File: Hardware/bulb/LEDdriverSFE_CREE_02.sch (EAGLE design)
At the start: 26 parts, among them U1 ZXLD1360, U2 ZXLD1360, U3 ZXLD1360, U4 ZXLD1360

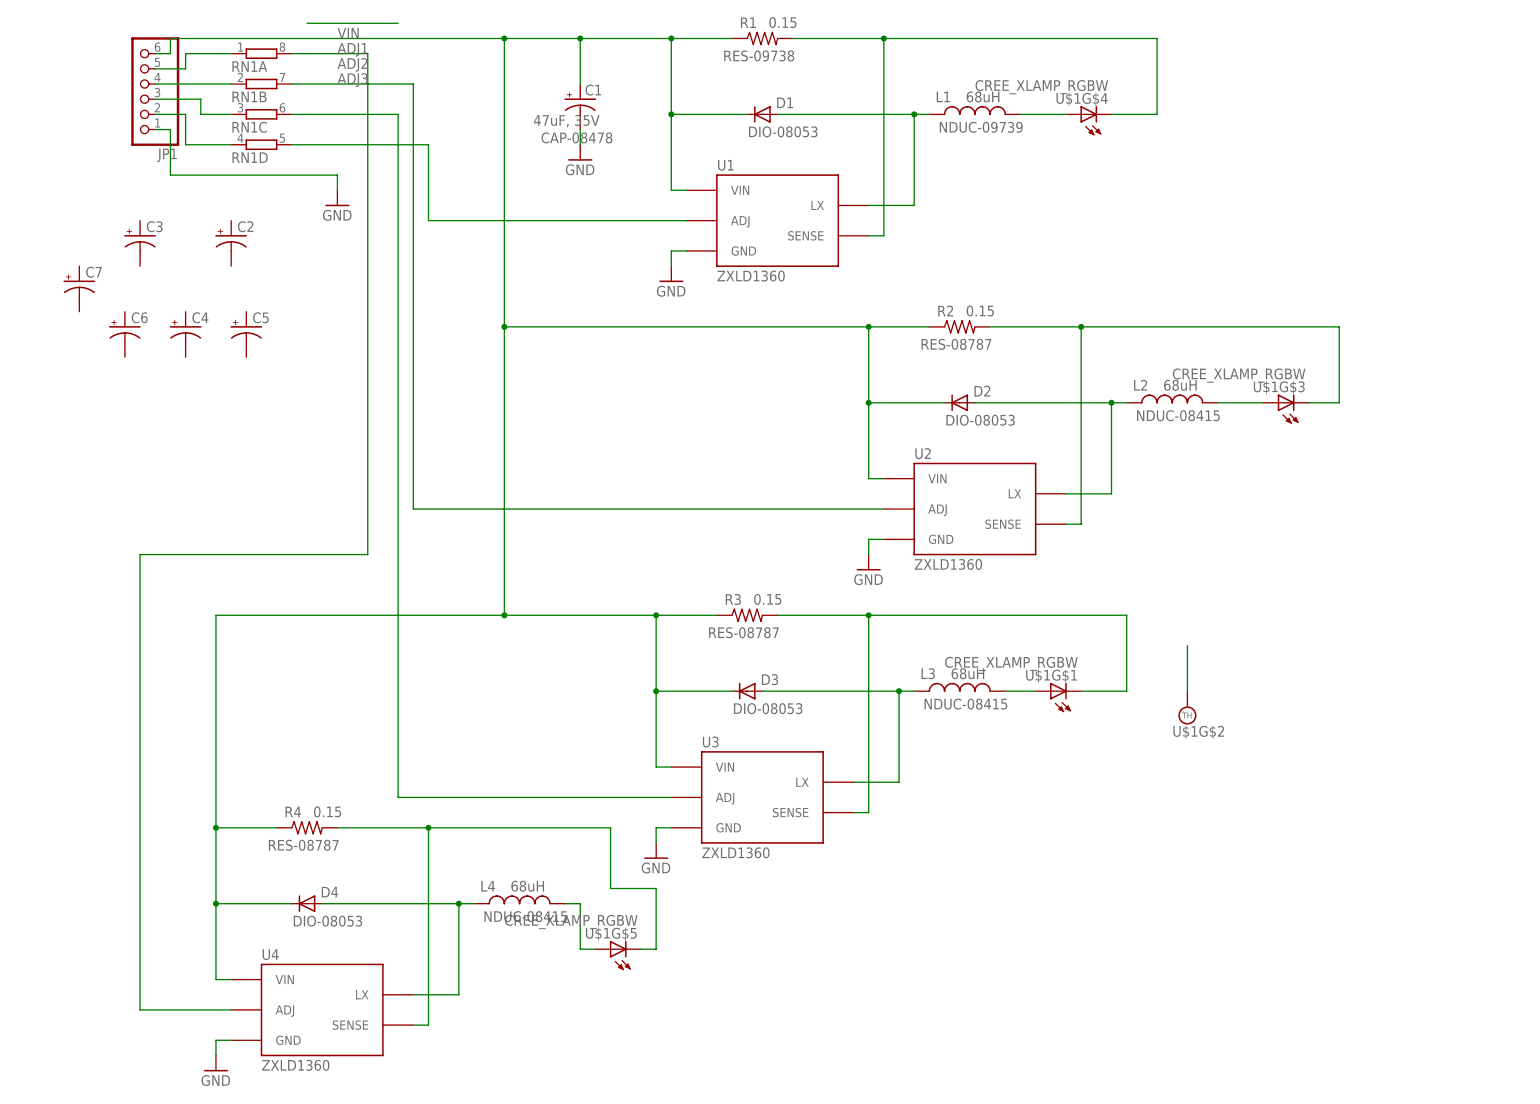
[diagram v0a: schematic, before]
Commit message: added firmware version 08 and included updates to server
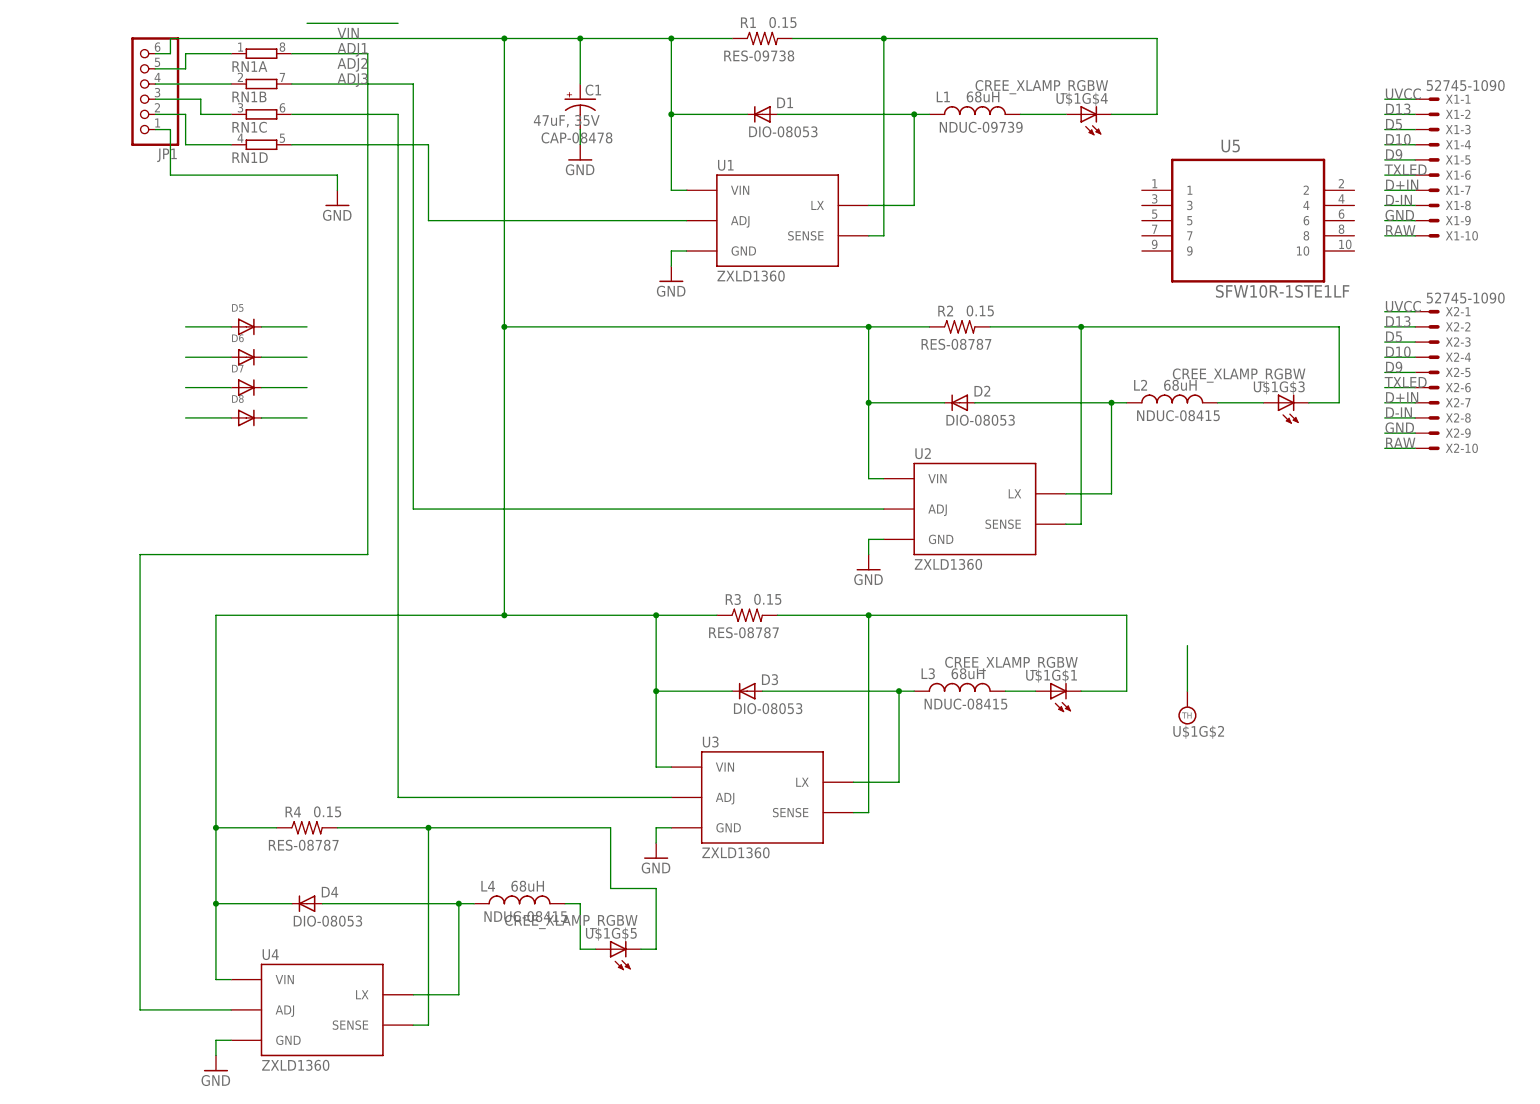
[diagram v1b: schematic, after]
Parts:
- removed C2: (no value), rcl:CPOL-USB
- removed C3: (no value), rcl:CPOL-US153CLV-0605
- removed C4: (no value), rcl:CPOL-US153CLV-0505
- removed C5: (no value), rcl:CPOL-USC
- removed C6: (no value), rcl:CPOL-US153CLV-0807
- removed C7: (no value), rcl:CPOL-US175TMP-0808
- added D5, D6, D7, D8: (no value), adafruit:DIODESOD-323F
- added U5: SFW10R-1STE1LF, FCI_By_element14_Batch_1:SFW10R-1STE1LF
- added X1, X2: 52745-1090, con-molex:52745-1090
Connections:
- removed net N$15: JP1.5, RN1A.1
- removed net N$18: JP1.3, RN1C.1
- new net BLUEIN: D7.C, JP1.4, RN1B.1
- new net D+IN: X1-7.S, X2-7.S
- new net D-IN: X1-8.S, X2-8.S
- new net D10: X1-4.S, X2-4.S
- new net D13: X1-2.S, X2-2.S
- new net D5: X1-3.S, X2-3.S
- new net D9: X1-5.S, X2-5.S
- new net GREENIN: D6.C, JP1.2, RN1D.1
- new net N$20: D7.A
- new net N$21: D8.A
- new net RAW: X1-10.S, X2-10.S
- new net REDIN: D5.C, JP1.5, RN1A.1
- new net TXLED: X1-6.S, X2-6.S
- new net UVCC: X1-1.S, X2-1.S
- new net WHITEIN: D8.C, JP1.3, RN1C.1
- net GND: now also X1-9.S, X2-9.S
- net N$14: now also D5.A; no longer JP1.2, RN1D.1
- net N$17: now also D6.A; no longer JP1.4, RN1B.1
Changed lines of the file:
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@@
 <?xml version="1.0" encoding="utf-8"?>
 <!DOCTYPE eagle SYSTEM "eagle.dtd">
-<eagle version="6.2">
+<eagle version="6.4">
 <drawing>
 <settings>
@@
 <class number="0" name="default" width="0" drill="0">
 </class>
+<class number="1" name="vcc" width="0" drill="0">
+</class>
 </classes>
 <parts>
@@
 <part name="JP1" library="adafruit" deviceset="PINHD-1X6" device=""/>
 <part name="RN1" library="resistor-dil" deviceset="4R-N" device="EXBV8V"/>
-<part name="C2" library="rcl" deviceset="CPOL-US" device="B"/>
-<part name="C3" library="rcl" deviceset="CPOL-US" device="153CLV-0605"/>
-<part name="C4" library="rcl" deviceset="CPOL-US" device="153CLV-0505"/>
-<part name="C5" library="rcl" deviceset="CPOL-US" device="C"/>
-<part name="C6" library="rcl" deviceset="CPOL-US" device="153CLV-0807"/>
-<part name="C7" library="rcl" deviceset="CPOL-US" device="175TMP-0808"/>
+<part name="D5" library="adafruit" deviceset="DIODE" device="SOD-323F"/>
+<part name="D6" library="adafruit" deviceset="DIODE" device="SOD-323F"/>
+<part name="D7" library="adafruit" deviceset="DIODE" device="SOD-323F"/>
+<part name="D8" library="adafruit" deviceset="DIODE" device="SOD-323F"/>
+<part name="X1" library="con-molex" deviceset="52745-1090" device=""/>
+<part name="X2" library="con-molex" deviceset="52745-1090" device=""/>
+<part name="U5" library="FCI_By_element14_Batch_1" deviceset="SFW10R-1STE1LF" device=""/>
 </parts>
 <sheets>
@@
 <instance part="RN1" gate="C" x="35.56" y="165.1"/>
 <instance part="RN1" gate="D" x="35.56" y="160.02"/>
-<instance part="C2" gate="G$1" x="30.48" y="144.78"/>
-<instance part="C3" gate="G$1" x="15.24" y="144.78"/>
-<instance part="C4" gate="G$1" x="22.86" y="129.54"/>
-<instance part="C5" gate="G$1" x="33.02" y="129.54"/>
-<instance part="C6" gate="G$1" x="12.7" y="129.54"/>
-<instance part="C7" gate="G$1" x="5.08" y="137.16"/>
+<instance part="D5" gate="G$1" x="33.02" y="129.54"/>
+<instance part="D6" gate="G$1" x="33.02" y="124.46"/>
+<instance part="D7" gate="G$1" x="33.02" y="119.38"/>
+<instance part="D8" gate="G$1" x="33.02" y="114.3"/>
+<instance part="X1" gate="-1" x="231.14" y="167.64"/>
+<instance part="X1" gate="-2" x="231.14" y="165.1"/>
+<instance part="X1" gate="-3" x="231.14" y="162.56"/>
+<instance part="X1" gate="-4" x="231.14" y="160.02"/>
+<instance part="X1" gate="-5" x="231.14" y="157.48"/>
+<instance part="X1" gate="-6" x="231.14" y="154.94"/>
+<instance part="X1" gate="-7" x="231.14" y="152.4"/>
+<instance part="X1" gate="-8" x="231.14" y="149.86"/>
+<instance part="X1" gate="-9" x="231.14" y="147.32"/>
+<instance part="X1" gate="-10" x="231.14" y="144.78"/>
+<instance part="X2" gate="-1" x="231.14" y="132.08"/>
+<instance part="X2" gate="-2" x="231.14" y="129.54"/>
+<instance part="X2" gate="-3" x="231.14" y="127"/>
+<instance part="X2" gate="-4" x="231.14" y="124.46"/>
+<instance part="X2" gate="-5" x="231.14" y="121.92"/>
+<instance part="X2" gate="-6" x="231.14" y="119.38"/>
+<instance part="X2" gate="-7" x="231.14" y="116.84"/>
+<instance part="X2" gate="-8" x="231.14" y="114.3"/>
+<instance part="X2" gate="-9" x="231.14" y="111.76"/>
+<instance part="X2" gate="-10" x="231.14" y="109.22"/>
+<instance part="U5" gate="A" x="200.66" y="149.86"/>
 </instances>
 <busses>
@@
 <pinref part="U4" gate="G$1" pin="GND"/>
 <pinref part="GND6" gate="1" pin="GND"/>
+</segment>
+<segment>
+<pinref part="X1" gate="-9" pin="S"/>
+<wire x1="228.6" y1="147.32" x2="223.52" y2="147.32" width="0.1524" layer="91"/>
+<label x="223.52" y="147.32" size="1.778" layer="95"/>
+</segment>
+<segment>
+<pinref part="X2" gate="-9" pin="S"/>
+<wire x1="228.6" y1="111.76" x2="223.52" y2="111.76" width="0.1524" layer="91"/>
+<label x="223.52" y="111.76" size="1.778" layer="95"/>
 </segment>
 </net>
@@
 </segment>
 </net>
-<net name="N$14" class="0">
+<net name="GREENIN" class="0">
 <segment>
 <pinref part="RN1" gate="D" pin="1"/>
@@
 <wire x1="22.86" y1="165.1" x2="17.78" y2="165.1" width="0.1524" layer="91"/>
 </segment>
-</net>
-<net name="N$15" class="0">
+<segment>
+<pinref part="D6" gate="G$1" pin="C"/>
+<wire x1="35.56" y1="124.46" x2="43.18" y2="124.46" width="0.1524" layer="91"/>
+</segment>
+</net>
+<net name="REDIN" class="0">
 <segment>
 <pinref part="RN1" gate="A" pin="1"/>
@@
 <wire x1="22.86" y1="172.72" x2="17.78" y2="172.72" width="0.1524" layer="91"/>
 </segment>
-</net>
-<net name="N$17" class="0">
+<segment>
+<pinref part="D5" gate="G$1" pin="C"/>
+<wire x1="35.56" y1="129.54" x2="43.18" y2="129.54" width="0.1524" layer="91"/>
+</segment>
+</net>
+<net name="BLUEIN" class="0">
 <segment>
 <pinref part="RN1" gate="B" pin="1"/>
@@
 <wire x1="30.48" y1="170.18" x2="17.78" y2="170.18" width="0.1524" layer="91"/>
 </segment>
-</net>
-<net name="N$18" class="0">
+<segment>
+<pinref part="D7" gate="G$1" pin="C"/>
+<wire x1="35.56" y1="119.38" x2="43.18" y2="119.38" width="0.1524" layer="91"/>
+</segment>
+</net>
+<net name="WHITEIN" class="0">
 <segment>
 <pinref part="RN1" gate="C" pin="1"/>
@@
 <wire x1="25.4" y1="167.64" x2="17.78" y2="167.64" width="0.1524" layer="91"/>
 </segment>
+<segment>
+<pinref part="D8" gate="G$1" pin="C"/>
+<wire x1="35.56" y1="114.3" x2="43.18" y2="114.3" width="0.1524" layer="91"/>
+</segment>
 </net>
 <net name="N$1" class="0">
@@
 </segment>
 </net>
+<net name="N$14" class="0">
+<segment>
+<pinref part="D5" gate="G$1" pin="A"/>
+<wire x1="30.48" y1="129.54" x2="22.86" y2="129.54" width="0.1524" layer="91"/>
+</segment>
+</net>
+<net name="N$17" class="0">
+<segment>
+<pinref part="D6" gate="G$1" pin="A"/>
+<wire x1="30.48" y1="124.46" x2="22.86" y2="124.46" width="0.1524" layer="91"/>
+</segment>
+</net>
+<net name="N$20" class="0">
+<segment>
+<pinref part="D7" gate="G$1" pin="A"/>
+<wire x1="30.48" y1="119.38" x2="22.86" y2="119.38" width="0.1524" layer="91"/>
+</segment>
+</net>
+<net name="N$21" class="0">
+<segment>
+<pinref part="D8" gate="G$1" pin="A"/>
+<wire x1="30.48" y1="114.3" x2="22.86" y2="114.3" width="0.1524" layer="91"/>
+</segment>
+</net>
+<net name="D9" class="0">
+<segment>
+<pinref part="X1" gate="-5" pin="S"/>
+<wire x1="228.6" y1="157.48" x2="223.52" y2="157.48" width="0.1524" layer="91"/>
+<label x="223.52" y="157.48" size="1.778" layer="95"/>
+</segment>
+<segment>
+<pinref part="X2" gate="-5" pin="S"/>
+<wire x1="228.6" y1="121.92" x2="223.52" y2="121.92" width="0.1524" layer="91"/>
+<label x="223.52" y="121.92" size="1.778" layer="95"/>
+</segment>
+</net>
+<net name="D5" class="0">
+<segment>
+<pinref part="X1" gate="-3" pin="S"/>
+<wire x1="228.6" y1="162.56" x2="223.52" y2="162.56" width="0.1524" layer="91"/>
+<label x="223.52" y="162.56" size="1.778" layer="95"/>
+</segment>
+<segment>
+<pinref part="X2" gate="-3" pin="S"/>
+<wire x1="228.6" y1="127" x2="223.52" y2="127" width="0.1524" layer="91"/>
+<label x="223.52" y="127" size="1.778" layer="95"/>
+</segment>
+</net>
+<net name="D10" class="0">
+<segment>
+<pinref part="X1" gate="-4" pin="S"/>
+<wire x1="228.6" y1="160.02" x2="223.52" y2="160.02" width="0.1524" layer="91"/>
+<label x="223.52" y="160.02" size="1.778" layer="95"/>
+</segment>
+<segment>
+<pinref part="X2" gate="-4" pin="S"/>
+<wire x1="228.6" y1="124.46" x2="223.52" y2="124.46" width="0.1524" layer="91"/>
+<label x="223.52" y="124.46" size="1.778" layer="95"/>
+</segment>
+</net>
+<net name="UVCC" class="0">
+<segment>
+<pinref part="X1" gate="-1" pin="S"/>
+<wire x1="228.6" y1="167.64" x2="223.52" y2="167.64" width="0.1524" layer="91"/>
+<label x="223.52" y="167.64" size="1.778" layer="95"/>
+</segment>
+<segment>
+<pinref part="X2" gate="-1" pin="S"/>
+<wire x1="228.6" y1="132.08" x2="223.52" y2="132.08" width="0.1524" layer="91"/>
+<label x="223.52" y="132.08" size="1.778" layer="95"/>
+</segment>
+</net>
+<net name="D13" class="0">
+<segment>
+<pinref part="X1" gate="-2" pin="S"/>
+<wire x1="228.6" y1="165.1" x2="223.52" y2="165.1" width="0.1524" layer="91"/>
+<label x="223.52" y="165.1" size="1.778" layer="95"/>
+</segment>
+<segment>
+<pinref part="X2" gate="-2" pin="S"/>
+<wire x1="228.6" y1="129.54" x2="223.52" y2="129.54" width="0.1524" layer="91"/>
+<label x="223.52" y="129.54" size="1.778" layer="95"/>
+</segment>
+</net>
+<net name="TXLED" class="0">
+<segment>
+<pinref part="X1" gate="-6" pin="S"/>
+<wire x1="228.6" y1="154.94" x2="223.52" y2="154.94" width="0.1524" layer="91"/>
+<label x="223.52" y="154.94" size="1.778" layer="95"/>
+</segment>
+<segment>
+<pinref part="X2" gate="-6" pin="S"/>
+<wire x1="228.6" y1="119.38" x2="223.52" y2="119.38" width="0.1524" layer="91"/>
+<label x="223.52" y="119.38" size="1.778" layer="95"/>
+</segment>
+</net>
+<net name="RAW" class="0">
+<segment>
+<pinref part="X1" gate="-10" pin="S"/>
+<wire x1="228.6" y1="144.78" x2="223.52" y2="144.78" width="0.1524" layer="91"/>
+<label x="223.52" y="144.78" size="1.778" layer="95"/>
+</segment>
+<segment>
+<pinref part="X2" gate="-10" pin="S"/>
+<wire x1="228.6" y1="109.22" x2="223.52" y2="109.22" width="0.1524" layer="91"/>
+<label x="223.52" y="109.22" size="1.778" layer="95"/>
+</segment>
+</net>
+<net name="D+IN" class="0">
+<segment>
+<pinref part="X1" gate="-7" pin="S"/>
+<wire x1="228.6" y1="152.4" x2="223.52" y2="152.4" width="0.1524" layer="91"/>
+<label x="223.52" y="152.4" size="1.778" layer="95"/>
+</segment>
+<segment>
+<pinref part="X2" gate="-7" pin="S"/>
+<wire x1="228.6" y1="116.84" x2="223.52" y2="116.84" width="0.1524" layer="91"/>
+<label x="223.52" y="116.84" size="1.778" layer="95"/>
+</segment>
+</net>
+<net name="D-IN" class="0">
+<segment>
+<pinref part="X1" gate="-8" pin="S"/>
+<wire x1="228.6" y1="149.86" x2="223.52" y2="149.86" width="0.1524" layer="91"/>
+<label x="223.52" y="149.86" size="1.778" layer="95"/>
+</segment>
+<segment>
+<pinref part="X2" gate="-8" pin="S"/>
+<wire x1="228.6" y1="114.3" x2="223.52" y2="114.3" width="0.1524" layer="91"/>
+<label x="223.52" y="114.3" size="1.778" layer="95"/>
+</segment>
+</net>

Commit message: updates to api docs and file
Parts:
- removed JP1: (no value), adafruit:PINHD-1X6
- removed U5: SFW10R-1STE1LF, FCI_By_element14_Batch_1:SFW10R-1STE1LF
- removed X2: 52745-1090, con-molex:52745-1090
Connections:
- net ADJ3 renamed WHITE
- removed net ADJ1: RN1D.2, U1.ADJ
- removed net ADJ2: RN1B.2, U2.ADJ
- removed net BLUEIN: D7.C, JP1.4, RN1B.1
- removed net GREENIN: D6.C, JP1.2, RN1D.1
- removed net N$13: RN1A.2, U4.ADJ
- removed net N$14: D5.A
- removed net N$17: D6.A
- removed net N$20: D7.A
- removed net N$21: D8.A
- removed net RAW: X1-10.S, X2-10.S
- removed net REDIN: D5.C, JP1.5, RN1A.1
- removed net WHITEIN: D8.C, JP1.3, RN1C.1
- new net BLUE: RN1A.2, U2.ADJ
- new net GREEN: RN1B.2, U1.ADJ
- new net RED: RN1D.2, U4.ADJ
- net D+IN: now also X1-4.S; no longer X1-7.S, X2-7.S
- net D-IN: now also X1-3.S; no longer X1-8.S, X2-8.S
- net D10: now also D6.C, RN1B.1, X1-7.S; no longer X1-4.S, X2-4.S
- net D13: now also D7.C, RN1D.1, X1-9.S; no longer X1-2.S, X2-2.S
- net D5: now also D8.C, RN1C.1, X1-8.S; no longer X1-3.S, X2-3.S
- net D9: now also D5.C, RN1A.1, X1-6.S; no longer X1-5.S, X2-5.S
- net GND: now also D5.A, D6.A, D7.A, D8.A, X1-2.S; no longer JP1.1, X1-9.S, X2-9.S
- net TXLED: now also X1-5.S; no longer X1-6.S, X2-6.S
- net UVCC: now also X1-10.S; no longer X1-1.S, X2-1.S
- net VIN: now also X1-1.S; no longer JP1.6
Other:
- moved on the sheet: X1-1, X1-10, X1-2, X1-3, X1-4, X1-5, X1-6, X1-7, X1-8, X1-9
